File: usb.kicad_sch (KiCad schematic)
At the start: 69 parts, among them J13 USB-C_GCT_USB4105-GF-A, J3 USB-C_GCT_USB4105-GF-A, Q1 SSM3J332R, Q3 BCM857BS-7-F, Q4 SSM3J332R, Q5 BCM857BS-7-F, Q7 BC817-25W, U11 AP22652W6, U15 AP22652W6, U2 TPD4E05U06QDQARQ1, U4 AP62301_TSOT, U5 TPD4E05U06QDQARQ1, U8 AP62301_TSOT

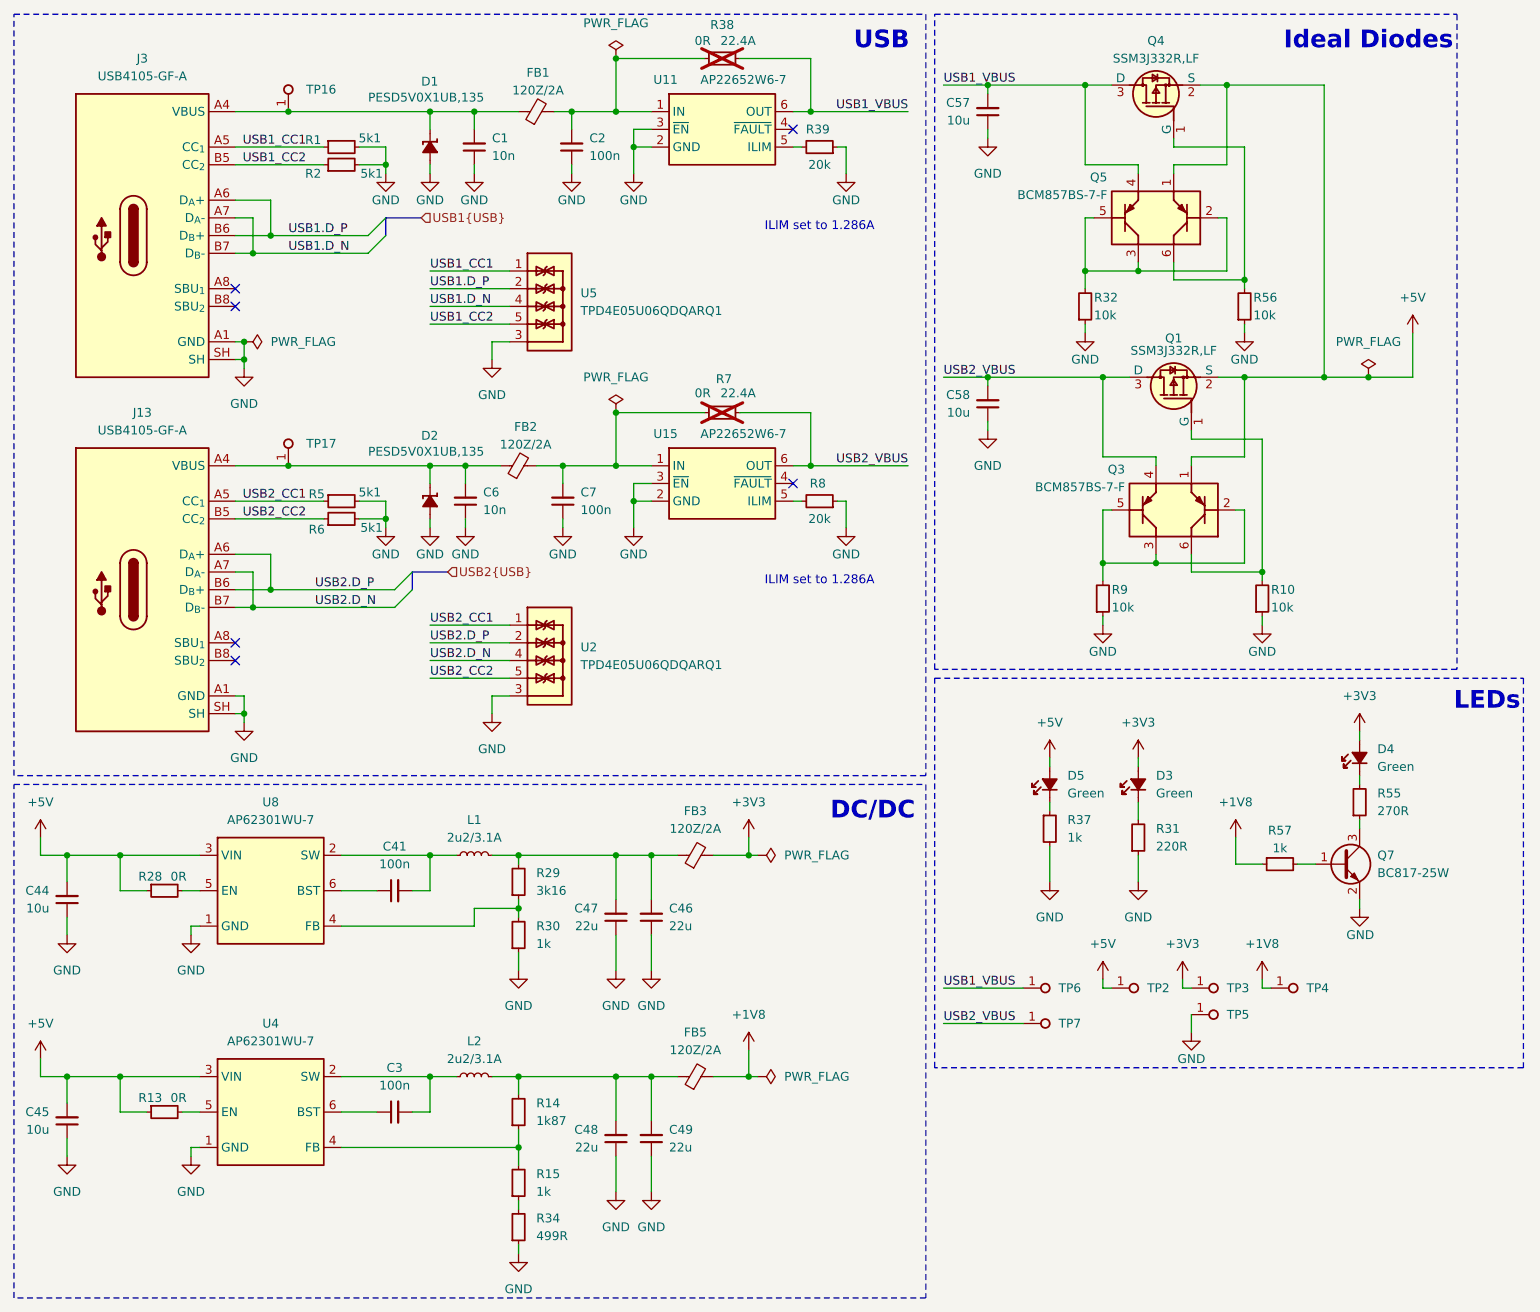
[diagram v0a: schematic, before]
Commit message: [#71986] Remove 1V8 circuits after changing the AMP
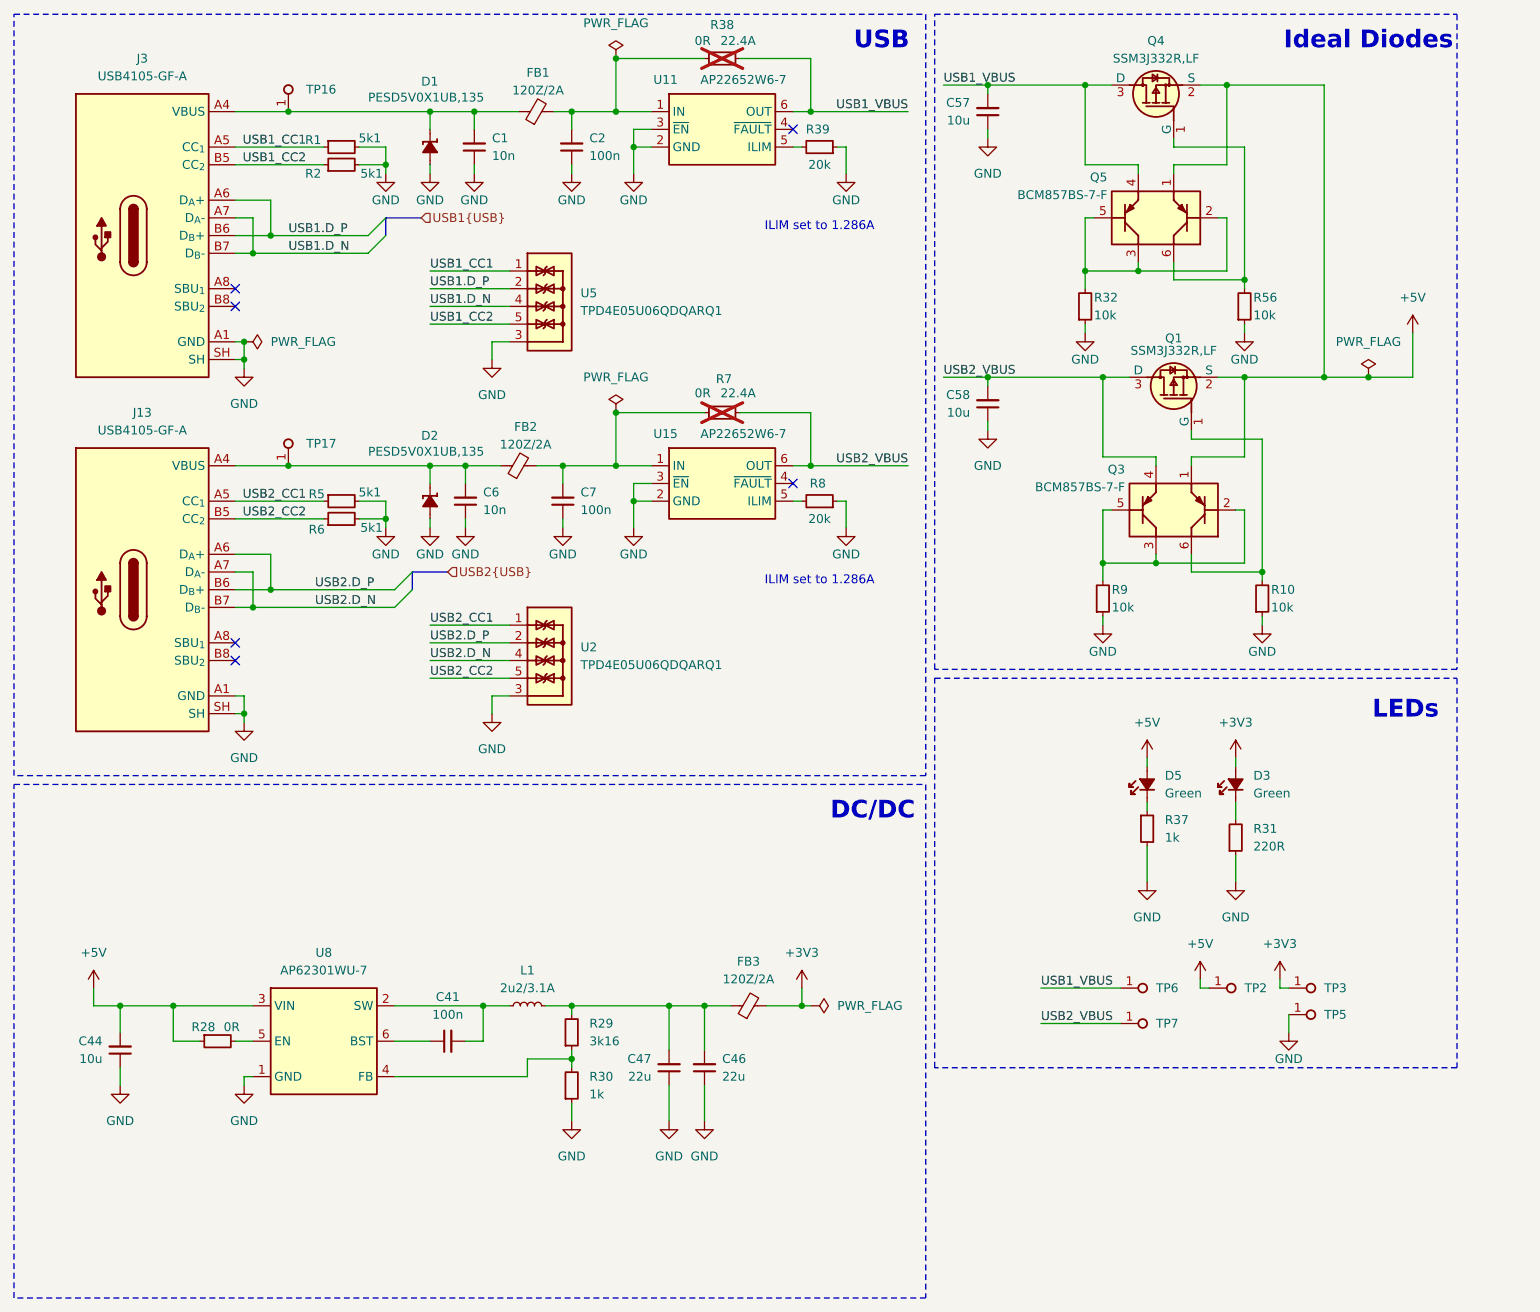
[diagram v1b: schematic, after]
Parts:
- removed C3: C_100n_0402, antmicro-footprints:C_0402_1005Metric, symbol antmicroCapacitors0402:C_100n_0402
- removed C45: C_10u_10V_0402, antmicro-footprints:C_0402_1005Metric, symbol antmicroCapacitors0402:C_10u_10V_0402
- removed C48, C49: C_22u_0402, antmicro-footprints:C_0402_1005Metric, symbol antmicroCapacitors0402:C_22u_0402
- removed D4: LED_G_0402_VLMTG1500-GS08, antmicro-footprints:LED_0402_1005Metric_G, symbol antmicroLEDIndicationDiscrete:LED_G_0402_VLMTG1500-GS08
- removed FB5: FB_120Z_2A_Murata-BLM18PG_0603, antmicro-footprints:FB_0603_1608Metric, symbol antmicroFerriteBeadsandChips:FB_120Z_2A_Murata-BLM18PG_0603
- removed L2: L_2u2_3.1A_Vishay-IFSC-1515AH-01, antmicro-footprints:L_Vishay-IFSC-1515AH, symbol antmicroFixedInductors:L_2u2_3.1A_Vishay-IFSC-1515AH-01
- removed Q7: BC817-25W, antmicro-footprints:SOT-323, symbol antmicroTransistorsBipolarSingle:BC817-25W
- removed R13: R_0R_0402, antmicro-footprints:R_0402_1005Metric, symbol antmicroResistors0402:R_0R_0402
- removed R14: R_1k87_0402, antmicro-footprints:R_0402_1005Metric, symbol antmicroResistors0402:R_1k87_0402
- removed R15, R57: R_1k_0402, antmicro-footprints:R_0402_1005Metric, symbol antmicroResistors0402:R_1k_0402
- removed R34: R_499R_0402, antmicro-footprints:R_0402_1005Metric, symbol antmicroResistors0402:R_499R_0402
- removed R55: R_270R_0402, antmicro-footprints:R_0402_1005Metric, symbol antmicroResistors0402:R_270R_0402
- removed TP4: TP_0.75mm_SMD, antmicro-footprints:TP_SMD_0.75mm, symbol antmicroTestPoints:TP_0.75mm_SMD
- removed U4: AP62301_TSOT, antmicro-footprints:TSOT23-6, symbol antmicroDCDCConverters:AP62301_TSOT
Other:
- moved on the sheet: C41, C44, C46, C47, D3, D5, FB3, L1, R28, R29, R30, R31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

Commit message: [#71249] Update project name
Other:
- title: Audio Latency Processing Board -> Audio controller board
